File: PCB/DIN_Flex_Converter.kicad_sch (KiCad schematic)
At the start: 36 parts, among them IC1 ZXTR2005Z-13, J1 Screw_Terminal_01x04, J2 Screw_Terminal_01x04, J3 Conn_01x04_Socket, J4 Conn_02x06_Top_Bottom, J5 Conn_02x06_Top_Bottom, U1 74HC04

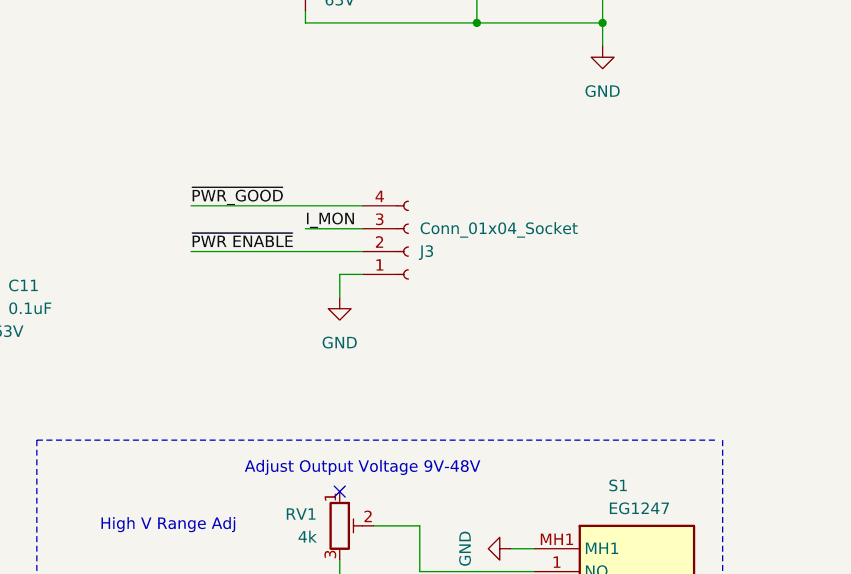
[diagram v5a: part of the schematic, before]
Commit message: fixed LED footprint/routing and added enable jumper
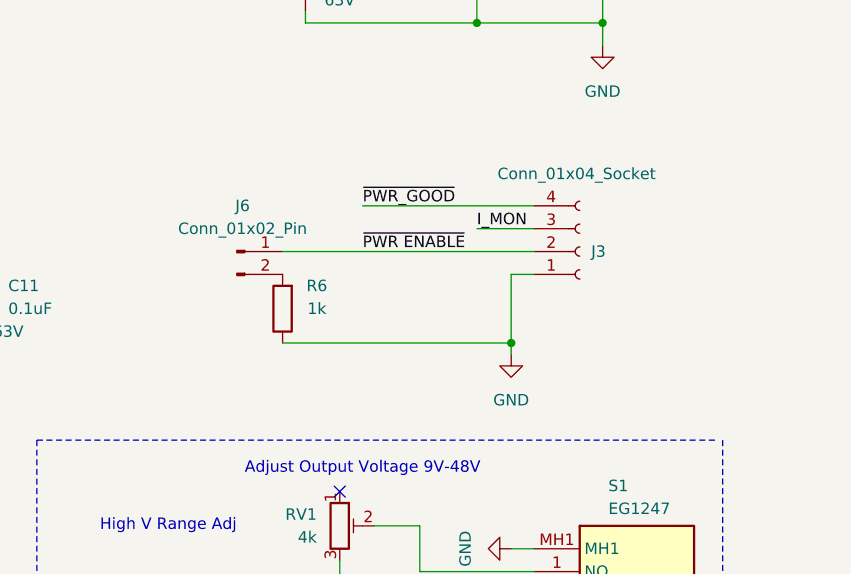
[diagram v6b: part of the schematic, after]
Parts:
- added J6: Conn_01x02_Pin, Connector_PinHeader_2.54mm:PinHeader_1x02_P2.54mm_Vertical, symbol Connector:Conn_01x02_Pin
- added R6: 1k, Resistor_SMD:R_1206_3216Metric, symbol Device:R
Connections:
- net GND: now also R6.1
- net ~{PWR ENABLE}: now also J6.1 (Pin_1)
- new net: J6.2 (Pin_2), R6.2
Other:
- moved on the sheet: J3
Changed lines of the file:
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@@
 		(color 0 0 0 0)
 	)
+	(junction
+		(at 257.81 101.6)
+		(diameter 0)
+		(color 0 0 0 0)
+	)
 	(no_connect
 		(at 124.46 130.81)
@@
 	(wire
 		(pts
-			(xy 222.25 86.36) (xy 241.3 86.36)
+			(xy 241.3 86.36) (xy 260.35 86.36)
 		)
 		(stroke
@@
 	(wire
 		(pts
+			(xy 257.81 101.6) (xy 257.81 93.98)
+		)
+		(stroke
+			(width 0)
+			(type default)
+		)
+	)
+	(wire
+		(pts
 			(xy 46.99 99.06) (xy 46.99 95.25)
 		)
@@
 	(wire
 		(pts
-			(xy 234.95 88.9) (xy 241.3 88.9)
+			(xy 254 88.9) (xy 260.35 88.9)
 		)
 		(stroke
@@
 	(wire
 		(pts
-			(xy 238.76 96.52) (xy 238.76 93.98)
+			(xy 257.81 102.87) (xy 257.81 101.6)
 		)
 		(stroke
@@
 	(wire
 		(pts
+			(xy 232.41 91.44) (xy 260.35 91.44)
+		)
+		(stroke
+			(width 0)
+			(type default)
+		)
+	)
+	(wire
+		(pts
 			(xy 113.03 46.99) (xy 113.03 54.61)
 		)
@@
 	(wire
 		(pts
+			(xy 232.41 101.6) (xy 257.81 101.6)
+		)
+		(stroke
+			(width 0)
+			(type default)
+		)
+	)
+	(wire
+		(pts
 			(xy 46.99 90.17) (xy 46.99 92.71)
 		)
@@
 	(wire
 		(pts
-			(xy 222.25 91.44) (xy 241.3 91.44)
-		)
-		(stroke
-			(width 0)
-			(type default)
-		)
-	)
-	(wire
-		(pts
 			(xy 242.57 121.92) (xy 247.65 121.92)
 		)
@@
 	(wire
 		(pts
-			(xy 238.76 93.98) (xy 241.3 93.98)
+			(xy 257.81 93.98) (xy 260.35 93.98)
 		)
 		(stroke
@@
 	)
 	(label "~{PWR_GOOD}"
-		(at 222.25 86.36 0)
+		(at 241.3 86.36 0)
 		(fields_autoplaced yes)
 		(effects
@@
 	)
 	(label "I_MON"
-		(at 234.95 88.9 0)
+		(at 254 88.9 0)
 		(fields_autoplaced yes)
 		(effects
@@
 	)
 	(label "~{PWR ENABLE}"
-		(at 222.25 91.44 0)
+		(at 241.3 91.44 0)
 		(fields_autoplaced yes)
 		(effects
@@
 	)
 	(symbol
+		(lib_id "Device:R")
+		(at 232.41 97.79 180)
+		(unit 1)
+		(exclude_from_sim no)
+		(in_bom yes)
+		(on_board yes)
+		(dnp no)
+		(property "Reference" "R6"
+			(at 236.22 95.25 0)
+			(effects
+				(font
+					(size 1.27 1.27)
+				)
+			)
+		)
+		(property "Value" "1k"
+			(at 236.22 97.79 0)
+			(effects
+				(font
+					(size 1.27 1.27)
+				)
+			)
+		)
+		(property "Footprint" "Resistor_SMD:R_1206_3216Metric"
+			(at 234.188 97.79 90)
+			(effects
+				(font
+					(size 1.27 1.27)
+				)
+				(hide yes)
+			)
+		)
+		(property "Datasheet" "~"
+			(at 232.41 97.79 0)
+			(effects
+				(font
+					(size 1.27 1.27)
+				)
+				(hide yes)
+			)
+		)
+		(property "Description" ""
+			(at 232.41 97.79 0)
+			(effects
+				(font
+					(size 1.27 1.27)
+				)
+				(hide yes)
+			)
+		)
+		(pin "1"
+		)
+		(pin "2"
+		)
+		(instances
+			(project "DIN_Flex_Converter"
+				(path "/e44269d9-3860-4750-a5c6-e30e8b477b13"
+					(reference "R6")
+					(unit 1)
+				)
+			)
+		)
+	)
+	(symbol
 		(lib_id "74xx:74HC04")
 		(at 116.84 152.4 0)
@@
 	(symbol
 		(lib_id "Connector:Conn_01x04_Socket")
-		(at 246.38 91.44 0)
+		(at 265.43 91.44 0)
 		(mirror x)
 		(unit 1)
@@
 		(dnp no)
 		(property "Reference" "J3"
-			(at 247.65 91.4401 0)
+			(at 266.7 91.4401 0)
 			(effects
 				(font
@@
 		)
 		(property "Value" "Conn_01x04_Socket"
-			(at 247.65 88.9001 0)
+			(at 256.286 82.804 0)
 			(effects
 				(font
@@
 		)
 		(property "Footprint" "PSA:PHOENIX_1803293"
-			(at 246.38 91.44 0)
+			(at 265.43 91.44 0)
 			(effects
 				(font
@@
 		)
 		(property "Datasheet" "~"
-			(at 246.38 91.44 0)
+			(at 265.43 91.44 0)
 			(effects
 				(font
@@
 		)
 		(property "Description" "Generic connector, single row, 01x04, script generated"
-			(at 246.38 91.44 0)
+			(at 265.43 91.44 0)
 			(effects
 				(font
@@
 	)
 	(symbol
+		(lib_id "Connector:Conn_01x02_Pin")
+		(at 227.33 91.44 0)
+		(unit 1)
+		(exclude_from_sim no)
+		(in_bom yes)
+		(on_board yes)
+		(dnp no)
+		(fields_autoplaced yes)
+		(property "Reference" "J6"
+			(at 227.965 86.36 0)
+			(effects
+				(font
+					(size 1.27 1.27)
+				)
+			)
+		)
+		(property "Value" "Conn_01x02_Pin"
+			(at 227.965 88.9 0)
+			(effects
+				(font
+					(size 1.27 1.27)
+				)
+			)
+		)
+		(property "Footprint" "Connector_PinHeader_2.54mm:PinHeader_1x02_P2.54mm_Vertical"
+			(at 227.33 91.44 0)
+			(effects
+				(font
+					(size 1.27 1.27)
+				)
+				(hide yes)
+			)
+		)
+		(property "Datasheet" "~"
+			(at 227.33 91.44 0)
+			(effects
+				(font
+					(size 1.27 1.27)
+				)
+				(hide yes)
+			)
+		)
+		(property "Description" "Generic connector, single row, 01x02, script generated"
+			(at 227.33 91.44 0)
+			(effects
+				(font
+					(size 1.27 1.27)
+				)
+				(hide yes)
+			)
+		)
+		(pin "1"
+		)
+		(pin "2"
+		)
+		(instances
+			(project "DIN_Flex_Converter"
+				(path "/e44269d9-3860-4750-a5c6-e30e8b477b13"
+					(reference "J6")
+					(unit 1)
+				)
+			)
+		)
+	)
+	(symbol
 		(lib_id "Device:R")
 		(at 107.95 102.87 180)
@@
 		(lib_name "GND_14")
 		(lib_id "power:GND")
-		(at 238.76 96.52 0)
+		(at 257.81 102.87 0)
 		(unit 1)
 		(exclude_from_sim no)
@@
 		(fields_autoplaced yes)
 		(property "Reference" "#PWR011"
-			(at 238.76 102.87 0)
+			(at 257.81 109.22 0)
 			(effects
 				(font
@@
 		)
 		(property "Value" "GND"
-			(at 238.76 101.6 0)
+			(at 257.81 107.95 0)
 			(effects
 				(font
@@
 		)
 		(property "Footprint" ""
-			(at 238.76 96.52 0)
+			(at 257.81 102.87 0)
 			(effects
 				(font
@@
 		)
 		(property "Datasheet" ""
-			(at 238.76 96.52 0)
+			(at 257.81 102.87 0)
 			(effects
 				(font
@@
 		)
 		(property "Description" ""
-			(at 238.76 96.52 0)
+			(at 257.81 102.87 0)
 			(effects
 				(font
